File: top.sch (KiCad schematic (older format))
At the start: 27 parts, among them J1 USB_B_Mini, J2 TC2030_NL, J3 FFC-0.5MM-6POS, J4 Port_1, J5 Port_2, U1 PMIC-LDO-XC6204B332MR_SOT23-5_, U2 LP2985-5.0, U3 ATmega328P-MU, U4 ADXL335, Y1 16MHz

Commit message: Choose more descriptive name
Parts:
- U4: symbol top-hemi-rescue:ADXL335-SparkfunSensors-top-hemi-rescue -> node-rescue:ADXL335-SparkfunSensors-node-rescue
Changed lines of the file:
@@
 EESchema Schematic File Version 4
-LIBS:top-hemi-cache
+LIBS:node-cache
 EELAYER 29 0
 EELAYER END
@@
 $EndComp
 $Comp
-L top-hemi-rescue:ADXL335-SparkfunSensors-top-hemi-rescue U?
+L node-rescue:ADXL335-SparkfunSensors-node-rescue U?
 U 1 1 5C9710AE
 P 8150 3150

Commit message: Replace 2x1 header footprint by port footprint
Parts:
- J4, J5: footprint Connector_PinHeader_2.54mm:PinHeader_1x02_P2.54mm_Vertical -> node:port
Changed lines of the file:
@@
 F 0 "J5" H 5080 1242 50  0000 L CNN
 F 1 "Port_2" H 5080 1151 50  0000 L CNN
-F 2 "Connector_PinHeader_2.54mm:PinHeader_1x02_P2.54mm_Vertical" H 5000 1250 50  0001 C CNN
+F 2 "node:port" H 5000 1250 50  0001 C CNN
 F 3 "~" H 5000 1250 50  0001 C CNN
 	1    5000 1250
@@
 F 0 "J4" H 5080 792 50  0000 L CNN
 F 1 "Port_1" H 5080 701 50  0000 L CNN
-F 2 "Connector_PinHeader_2.54mm:PinHeader_1x02_P2.54mm_Vertical" H 5000 800 50  0001 C CNN
+F 2 "node:port" H 5000 800 50  0001 C CNN
 F 3 "~" H 5000 800 50  0001 C CNN
 	1    5000 800

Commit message: Switch to WS2812D-F5 footprints
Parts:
- D2, D3: footprint Connector_PinHeader_2.54mm:PinHeader_1x04_P2.54mm_Vertical -> node:WS2812D-F5
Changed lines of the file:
@@
 F 0 "D3" H 8550 4650 50  0000 L CNN
 F 1 "LED 2" H 8800 4150 50  0000 L CNN
-F 2 "Connector_PinHeader_2.54mm:PinHeader_1x04_P2.54mm_Vertical" H 8800 4100 50  0001 L TNN
+F 2 "node:WS2812D-F5" H 8800 4100 50  0001 L TNN
 F 3 "https://www.adafruit.com/product/1938" H 8850 4025 50  0001 L TNN
 F 4 "1938" H 0   0   50  0001 C CNN "MPN"
@@
 F 0 "D2" H 7600 4650 50  0000 L CNN
 F 1 "LED 1" H 7850 4150 50  0000 L CNN
-F 2 "Connector_PinHeader_2.54mm:PinHeader_1x04_P2.54mm_Vertical" H 7850 4100 50  0001 L TNN
+F 2 "node:WS2812D-F5" H 7850 4100 50  0001 L TNN
 F 3 "https://www.adafruit.com/product/1938" H 7900 4025 50  0001 L TNN
 F 4 "1938" H 0   0   50  0001 C CNN "MPN"

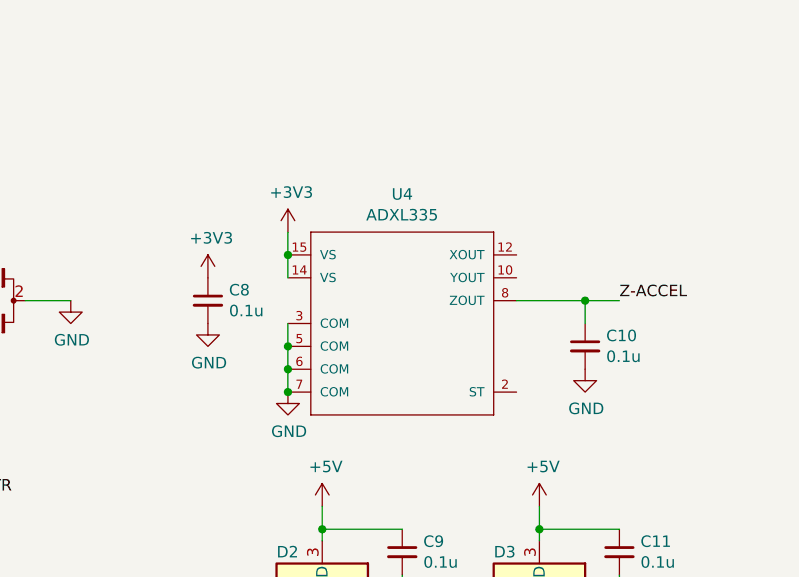
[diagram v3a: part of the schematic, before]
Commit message: Use ADXL335 from globally installed SparkFun lib
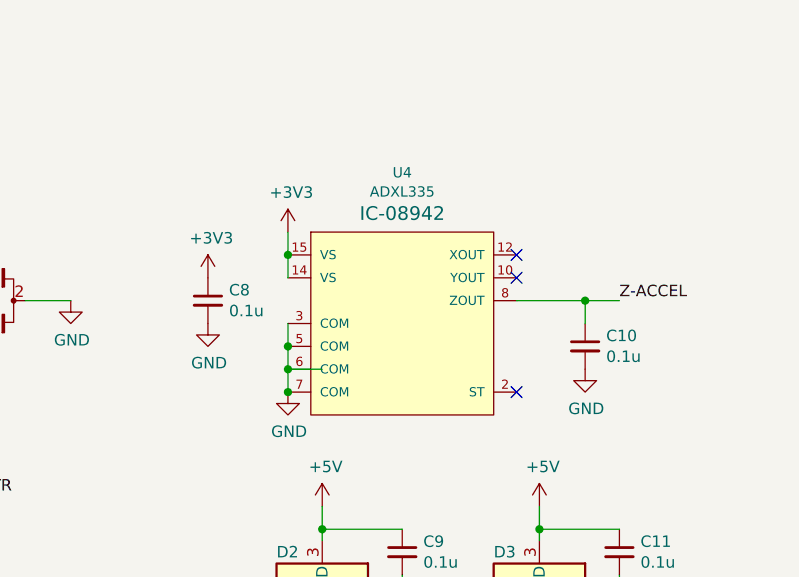
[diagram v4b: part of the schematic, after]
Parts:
- removed U4: ADXL335, Package_CSP:LFCSP-16-1EP_3x3mm_P0.5mm_EP1.6x1.6mm, symbol node-rescue:ADXL335-SparkfunSensors-node-rescue
- added U4: ADXL335, LFCSP-16-4X4, symbol SparkFun-Sensors:ADXL335
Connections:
- net +3V3: now also U4.14 (VS), U4.15 (VS)
- net GND: now also U4.3 (COM), U4.5 (COM), U4.6 (COM), U4.7 (COM)
- net Z-ACCEL: now also U4.8 (ZOUT)
- no-connect marks 0 -> 3
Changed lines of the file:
@@
 	1    0    0    -1
 $EndComp
-Wire Wire Line
-	7650 2850 7650 2950
-Connection ~ 7650 2850
-Wire Wire Line
-	7650 2750 7650 2850
 $Comp
 L power:+3V3 #PWR?
@@
 	1    0    0    -1
 $EndComp
-Wire Wire Line
-	7650 3350 7650 3450
-Connection ~ 7650 3350
-Wire Wire Line
-	7650 3250 7650 3350
-Connection ~ 7650 3250
-Connection ~ 7650 3450
-Wire Wire Line
-	7650 3150 7650 3250
 $Comp
 L power:GND #PWR?
@@
 F 7 "50" H 0   0   50  0001 C CNN "Min Quantity"
 	1    8950 3250
-	1    0    0    -1
-$EndComp
-$Comp
-L node-rescue:ADXL335-SparkfunSensors-node-rescue U?
-U 1 1 5C9710AE
-P 8150 3150
-AR Path="/5C9710AE" Ref="U?"  Part="1"
-AR Path="/5C920754/5C9710AE" Ref="U4"  Part="1"
-F 0 "U4" H 8150 3715 50  0000 C CNN
-F 1 "ADXL335" H 8150 3624 50  0000 C CNN
-F 2 "Package_CSP:LFCSP-16-1EP_3x3mm_P0.5mm_EP1.6x1.6mm" H 8180 3300 20  0001 C CNN
-F 3 "" H 8150 3150 50  0001 C CNN
-	1    8150 3150
 	1    0    0    -1
 $EndComp
@@
 	1900 5350 2000 5350
 Connection ~ 2000 5350
+Wire Wire Line
+	7650 2750 7650 2850
+$Comp
+L SparkFun-Sensors:ADXL335 U4
+U 1 1 5C9AF2E3
+P 8150 3150
+F 0 "U4" H 8150 3810 45  0000 C CNN
+F 1 "ADXL335" H 8150 3726 45  0000 C CNN
+F 2 "LFCSP-16-4X4" H 8150 3700 20  0001 C CNN
+F 3 "" H 8150 3150 60  0001 C CNN
+F 4 "IC-08942" H 8150 3631 60  0000 C CNN "Field4"
+	1    8150 3150
+	1    0    0    -1
+$EndComp
+Wire Wire Line
+	7650 3350 7650 3450
+Connection ~ 7650 3450
+Wire Wire Line
+	7800 3350 7650 3350
+Wire Wire Line
+	7650 3350 7650 3250
+Connection ~ 7650 3350
+Connection ~ 7650 3250
+Wire Wire Line
+	7650 3250 7650 3150
+Wire Wire Line
+	7650 2950 7650 2850
+Connection ~ 7650 2850
+NoConn ~ 8650 2850
+NoConn ~ 8650 2950
+NoConn ~ 8650 3450
 $EndSCHEMATC

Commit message: Fix: ADXL335 footprint too small (3x3 vs. 4x4)
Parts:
- U4: footprint LFCSP-16-4X4 -> (none)
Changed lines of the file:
@@
 F 0 "U4" H 8150 3810 45  0000 C CNN
 F 1 "ADXL335" H 8150 3726 45  0000 C CNN
-F 2 "LFCSP-16-4X4" H 8150 3700 20  0001 C CNN
+F 2 "" H 8150 3700 20  0001 C CNN
 F 3 "" H 8150 3150 60  0001 C CNN
 F 4 "IC-08942" H 8150 3631 60  0000 C CNN "Field4"

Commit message: Fix: footprint assignment not applied
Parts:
- U4: footprint (none) -> Package_CSP:LFCSP-16-1EP_4x4mm_P0.65mm_EP2.1x2.1mm
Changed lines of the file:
@@
 F 0 "U4" H 8150 3810 45  0000 C CNN
 F 1 "ADXL335" H 8150 3726 45  0000 C CNN
-F 2 "" H 8150 3700 20  0001 C CNN
+F 2 "Package_CSP:LFCSP-16-1EP_4x4mm_P0.65mm_EP2.1x2.1mm" H 8150 3700 20  0001 C CNN
 F 3 "" H 8150 3150 60  0001 C CNN
 F 4 "IC-08942" H 8150 3631 60  0000 C CNN "Field4"

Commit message: Switch to ADXL337: smaller & same pitch as 328P-MU
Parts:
- removed U4: ADXL335, Package_CSP:LFCSP-16-1EP_4x4mm_P0.65mm_EP2.1x2.1mm, symbol SparkFun-Sensors:ADXL335
- added U4: ADXL337, LFCSP-16-3X3, symbol SparkFun-Sensors:ADXL337
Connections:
- wire segments 82 -> 80
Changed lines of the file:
@@
 U 1 1 5CAD6264
 P 4600 3600
-F 0 "U3" H 4600 2011 50  0000 C CNN
-F 1 "ATmega328P-MU" H 4600 1920 50  0000 C CNN
+F 0 "U3" H 4150 5050 50  0000 C CNN
+F 1 "ATmega328P-MU" H 4950 2150 50  0000 C CNN
 F 2 "Package_DFN_QFN:QFN-32-1EP_5x5mm_P0.5mm_EP3.1x3.1mm" H 4600 3600 50  0001 C CIN
 F 3 "http://ww1.microchip.com/downloads/en/DeviceDoc/ATmega328_P%20AVR%20MCU%20with%20picoPower%20Technology%20Data%20Sheet%2040001984A.pdf" H 4600 3600 50  0001 C CNN
@@
 	1900 5350 2000 5350
 Connection ~ 2000 5350
+NoConn ~ 8650 2850
+NoConn ~ 8650 2950
+NoConn ~ 8650 3250
 Wire Wire Line
 	7650 2750 7650 2850
 $Comp
-L SparkFun-Sensors:ADXL335 U4
-U 1 1 5C9AF2E3
-P 8150 3150
-F 0 "U4" H 8150 3810 45  0000 C CNN
-F 1 "ADXL335" H 8150 3726 45  0000 C CNN
-F 2 "Package_CSP:LFCSP-16-1EP_4x4mm_P0.65mm_EP2.1x2.1mm" H 8150 3700 20  0001 C CNN
-F 3 "" H 8150 3150 60  0001 C CNN
-F 4 "IC-08942" H 8150 3631 60  0000 C CNN "Field4"
-	1    8150 3150
+L SparkFun-Sensors:ADXL337 U4
+U 1 1 5C9C6311
+P 8150 3050
+F 0 "U4" H 8150 3610 45  0000 C CNN
+F 1 "ADXL337" H 8150 3526 45  0000 C CNN
+F 2 "LFCSP-16-3X3" H 8150 3450 20  0001 C CNN
+F 3 "" H 8150 3050 60  0001 C CNN
+F 4 "IC-12011" H 8150 3431 60  0000 C CNN "Field4"
+	1    8150 3050
 	1    0    0    -1
 $EndComp
 Wire Wire Line
-	7650 3350 7650 3450
-Connection ~ 7650 3450
+	7650 2950 7650 2850
+Connection ~ 7650 2850
 Wire Wire Line
-	7800 3350 7650 3350
-Wire Wire Line
-	7650 3350 7650 3250
-Connection ~ 7650 3350
+	7650 3150 7650 3250
 Connection ~ 7650 3250
 Wire Wire Line
-	7650 3250 7650 3150
-Wire Wire Line
-	7650 2950 7650 2850
-Connection ~ 7650 2850
-NoConn ~ 8650 2850
-NoConn ~ 8650 2950
-NoConn ~ 8650 3450
+	7650 3250 7650 3450
 $EndSCHEMATC

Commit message: Assign footprint to ADXL337
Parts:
- U4: footprint LFCSP-16-3X3 -> Package_CSP:LFCSP-16-1EP_3x3mm_P0.5mm_EP1.6x1.6mm
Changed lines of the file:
@@
 F 0 "U4" H 8150 3610 45  0000 C CNN
 F 1 "ADXL337" H 8150 3526 45  0000 C CNN
-F 2 "LFCSP-16-3X3" H 8150 3450 20  0001 C CNN
+F 2 "Package_CSP:LFCSP-16-1EP_3x3mm_P0.5mm_EP1.6x1.6mm" H 8150 3450 20  0001 C CNN
 F 3 "" H 8150 3050 60  0001 C CNN
 F 4 "IC-12011" H 8150 3431 60  0000 C CNN "Field4"
